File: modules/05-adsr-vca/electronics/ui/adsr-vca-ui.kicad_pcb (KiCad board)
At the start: 2 copper layers, 58 x 110 mm, 36 parts, among them J1 Conn_02x03_Odd_Even, J3 Conn_02x03_Odd_Even, J4 Conn_01x02, J5 Conn_01x06, J6 Conn_02x03_Odd_Even, J8 Conn_02x03_Odd_Even, Q1 2N3904, Q2 2N3906

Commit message: ADSR+VCA UI JLCPCB verified for 1.0
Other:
- board text added: "SHMØERGH MODULEUR"
- board text added: "SM-05 ADSR VCA V1.0 2025 DEC"
- board text removed: "HM-05 ADSR VCA V0.2 2025 OCT"
- board text removed: "SHMØERGH HOG MODULEUR"

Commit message: Fixed pot part number bug in ADSR+VCA
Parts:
- RV_ATTACK1, RV_DECAY1, RV_RELEASE1: value A500k -> A200k-1M
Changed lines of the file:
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@@
 			)
 		)
-		(property "Value" "A500k"
+		(property "Value" "A200k-1M"
 			(at 0.1 13.379024 180)
 			(layer "F.Fab")
@@
 			)
 		)
-		(property "Part URL" "https://mou.sr/4694GMU"
+		(property "Part URL" "https://mou.sr/3VpxrOs"
 			(at 0 0 0)
 			(unlocked yes)
@@
 			)
 		)
-		(property "Part no." "652-PTV09A4025FB104"
+		(property "Part no." "652-PTV09A4025FA105 "
 			(at 0 0 0)
 			(unlocked yes)
@@
 			)
 		)
-		(property "Part URL" ""
+		(property "Part URL" "https://mou.sr/3MWzgkZ"
 			(at 0 0 0)
 			(unlocked yes)
@@
 			)
 		)
-		(property "Vendor" ""
+		(property "Vendor" "Mouser"
 			(at 0 0 0)
 			(unlocked yes)
@@
 			)
 		)
+		(property "Part no." "603-MFR-25FRF52-47K"
+			(at 0 0 0)
+			(unlocked yes)
+			(layer "F.Fab")
+			(hide yes)
+			(effects
+				(font
+					(size 1 1)
+					(thickness 0.15)
+				)
+			)
+		)
 		(property ki_fp_filters "R_*")
 		(sheetname "/")
@@
 			)
 		)
-		(property "Part URL" ""
+		(property "Part URL" "https://mou.sr/4a8lju1"
 			(at 0 0 180)
 			(unlocked yes)
@@
 			)
 		)
-		(property "Vendor" ""
+		(property "Vendor" "Mouser"
 			(at 0 0 180)
 			(unlocked yes)
@@
 			)
 		)
+		(property "Part no." "637-2N3906"
+			(at 0 0 180)
+			(unlocked yes)
+			(layer "F.Fab")
+			(hide yes)
+			(effects
+				(font
+					(size 1 1)
+					(thickness 0.15)
+				)
+			)
+		)
 		(property ki_fp_filters "TO?92*")
 		(sheetname "/")
@@
 			)
 		)
-		(property "Part URL" ""
+		(property "Part URL" "https://mou.sr/4hEwI4G"
 			(at 0 0 90)
 			(unlocked yes)
@@
 			)
 		)
-		(property "Vendor" ""
+		(property "Vendor" "Mouser"
 			(at 0 0 90)
 			(unlocked yes)
@@
 			)
 		)
+		(property "Part no." "603-MFR-25FRF52100K"
+			(at 0 0 90)
+			(unlocked yes)
+			(layer "F.Fab")
+			(hide yes)
+			(effects
+				(font
+					(size 1 1)
+					(thickness 0.15)
+				)
+			)
+		)
 		(property ki_fp_filters "R_*")
 		(sheetname "/")
@@
 			)
 		)
-		(property "Part URL" ""
+		(property "Part URL" "https://mou.sr/4q072Ei"
 			(at 0 0 0)
 			(unlocked yes)
@@
 			)
 		)
-		(property "Vendor" ""
+		(property "Vendor" "Mouser"
 			(at 0 0 0)
 			(unlocked yes)
@@
 			)
 		)
+		(property "Part no." "603-MFR25SFTF52-4K7"
+			(at 0 0 0)
+			(unlocked yes)
+			(layer "F.Fab")
+			(hide yes)
+			(effects
+				(font
+					(size 1 1)
+					(thickness 0.15)
+				)
+			)
+		)
 		(property ki_fp_filters "R_*")
 		(sheetname "/")
@@
 			)
 		)
-		(property "Part URL" ""
+		(property "Part URL" "https://mou.sr/4febysZ"
 			(at 0 0 270)
 			(unlocked yes)
@@
 			)
 		)
-		(property "Vendor" ""
+		(property "Vendor" "Mouser"
 			(at 0 0 270)
 			(unlocked yes)
@@
 			)
 		)
+		(property "Part no." "637-2N3904"
+			(at 0 0 270)
+			(unlocked yes)
+			(layer "F.Fab")
+			(hide yes)
+			(effects
+				(font
+					(size 1 1)
+					(thickness 0.15)
+				)
+			)
+		)
 		(property ki_fp_filters "TO?92*")
 		(sheetname "/")
@@
 			)
 		)
-		(property "Value" "A500k"
+		(property "Value" "A200k-1M"
 			(at 0.1 13.379024 180)
 			(layer "F.Fab")
@@
 			)
 		)
-		(property "Part URL" "https://mou.sr/4694GMU"
+		(property "Part URL" "https://mou.sr/3VpxrOs"
 			(at 0 0 0)
 			(unlocked yes)
@@
 			)
 		)
-		(property "Part no." "652-PTV09A4025FB104"
+		(property "Part no." "652-PTV09A4025FA105 "
 			(at 0 0 0)
 			(unlocked yes)
@@
 			)
 		)
-		(property "Part URL" "https://mou.sr/4694GMU"
+		(property "Part URL" "https://mou.sr/45PU5oa"
 			(at 0 0 90)
 			(unlocked yes)
@@
 			)
 		)
-		(property "Part no." "652-PTV09A4025FB104"
+		(property "Part no." "652-PTA4432015CPB103 "
 			(at 0 0 90)
 			(unlocked yes)
@@
 			)
 		)
-		(property "Value" "A500k"
+		(property "Value" "A200k-1M"
 			(at 0.1 13.379024 180)
 			(layer "F.Fab")
@@
 			)
 		)
-		(property "Part URL" "https://mou.sr/4694GMU"
+		(property "Part URL" "https://mou.sr/3VpxrOs"
 			(at 0 0 0)
 			(unlocked yes)
@@
 			)
 		)
-		(property "Part no." "652-PTV09A4025FB104"
+		(property "Part no." "652-PTV09A4025FA105 "
 			(at 0 0 0)
 			(unlocked yes)
@@
 			)
 		)
-		(property "Part URL" ""
+		(property "Part URL" "https://mou.sr/4nM6IZz"
 			(at 0 0 0)
 			(unlocked yes)
@@
 			)
 		)
-		(property "Vendor" ""
+		(property "Vendor" "Mouser"
 			(at 0 0 0)
 			(unlocked yes)
@@
 			(at 0 0 0)
 			(unlocked yes)
+			(layer "F.Fab")
+			(hide yes)
+			(effects
+				(font
+					(size 1 1)
+					(thickness 0.15)
+				)
+			)
+		)
+		(property "Part no." "200-HTSW10208TSRA"
+			(at 0 0 0)
+			(unlocked yes)

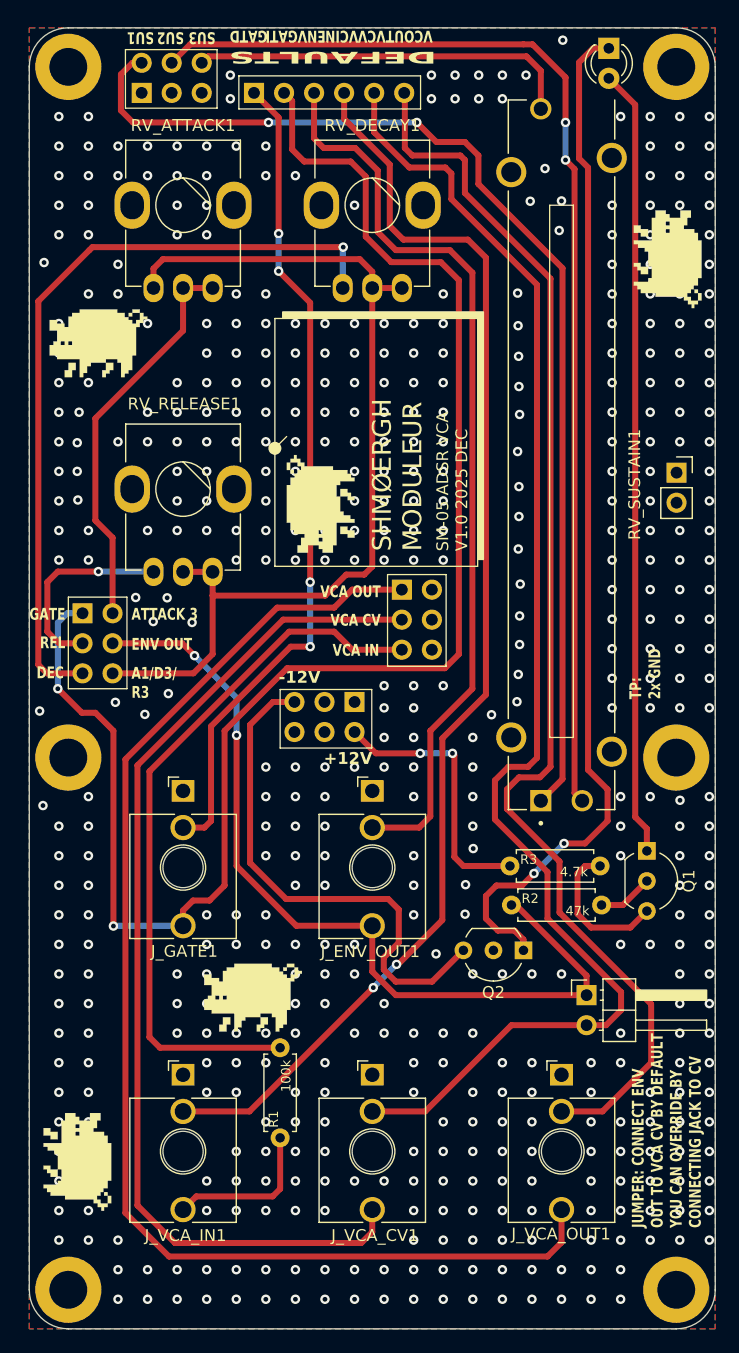
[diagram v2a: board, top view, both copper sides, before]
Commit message: Fixed missing resistor for VCA CV input
Boards before this commit missed a 200k resistor on the CV input of the VCA,
which caused the VCA to be very hot.

Additionally, we've added a small optional passive LP network to the CV input
to smoothen sudden changes on the CV input (which can cause very minor pops
on very short attack times for example).
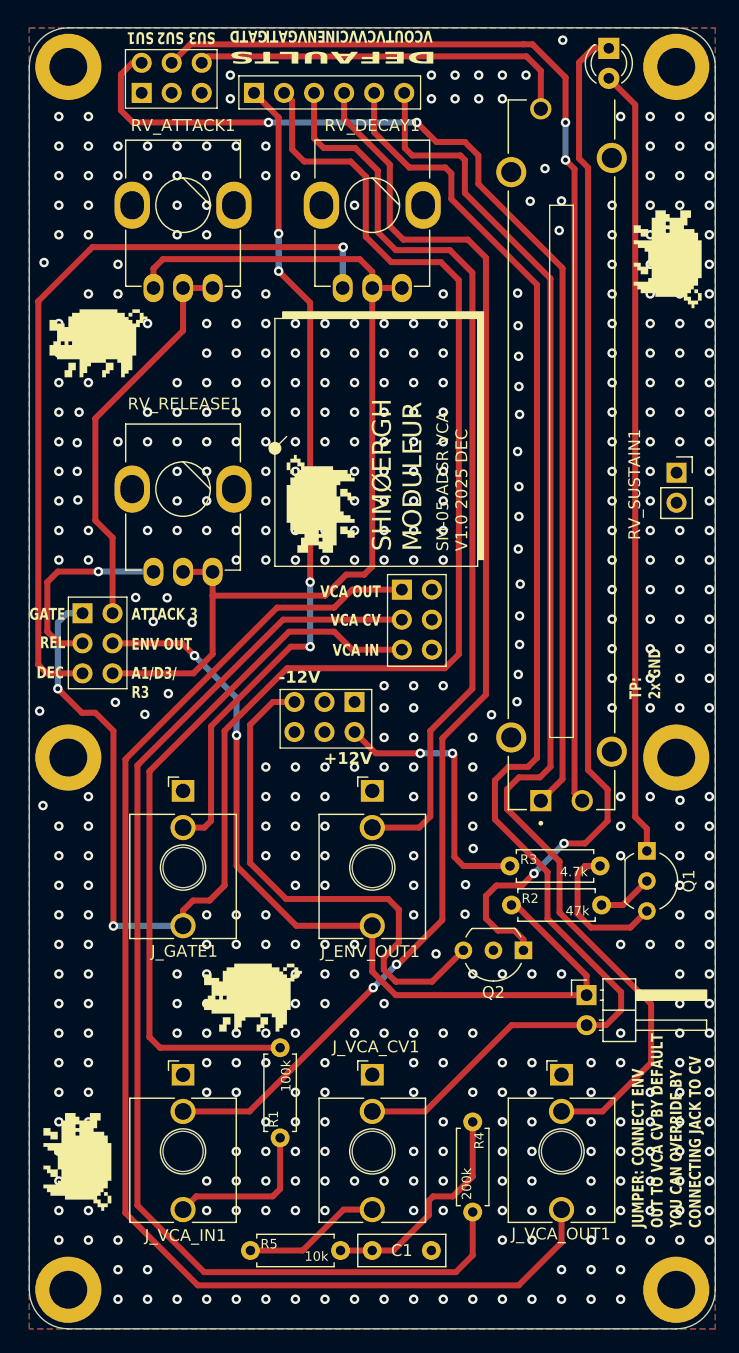
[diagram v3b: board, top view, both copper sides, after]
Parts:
- added C1: 100nF, Capacitor_THT:C_Rect_L7.2mm_W2.5mm_P5.00mm_FKS2_FKP2_MKS2_MKP2, F.Cu at (153.0, 147.4)
- added R4: 200k, Shmoergh_Custom_Footprints:R_Axial_DIN0207_L6.3mm_D2.5mm_P7.62mm_Horizontal, F.Cu at (161.5, 136.5)
- added R5: 10k, Shmoergh_Custom_Footprints:R_Axial_DIN0207_L6.3mm_D2.5mm_P7.62mm_Horizontal, F.Cu at (142.7, 147.4)
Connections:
- J_VCA_CV1 pad T: VCA_CV -> Net-(J_VCA_CV1-PadT)
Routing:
- net Net-(C1-Pad1): track 0.00 -> 19.1 mm
- net Net-(J_VCA_CV1-PadT): track 0.00 -> 11.7 mm
- net VCA_CV: track 88.1 -> 99.6 mm
- net VCA_OUT: track 109.3 -> 111.4 mm
- net GND: vias 521 -> 501

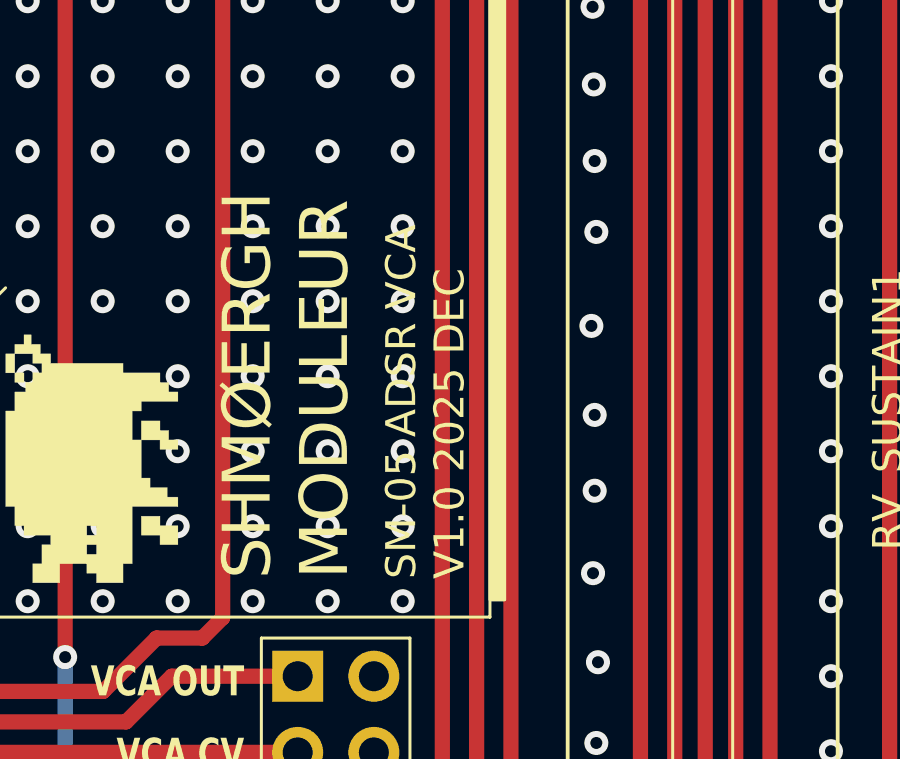
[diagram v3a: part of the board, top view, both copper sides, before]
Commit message: Updated VCA UI version to v1.1
This revision contains fix for missing resistor on VCA CV input,
and adds an optional LP filter for the CV input to avoid small pops
on sudden CV changes (e.g. very short attacks).
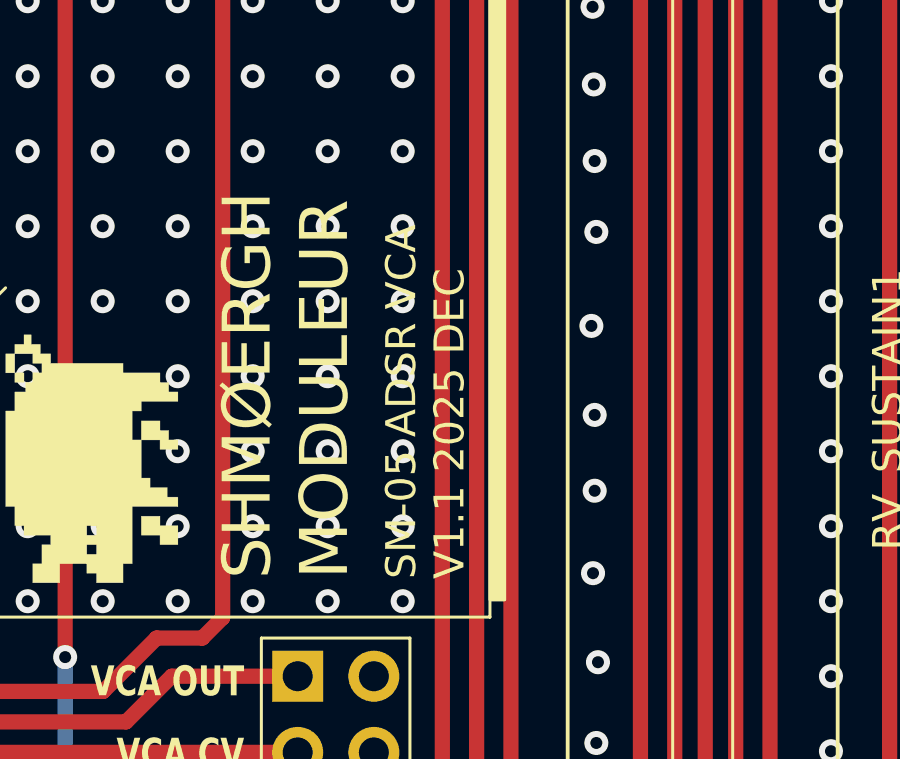
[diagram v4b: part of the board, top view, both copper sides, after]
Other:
- board text added: "SM-05 ADSR VCA V1.1 2025 DEC"
- board text removed: "SM-05 ADSR VCA V1.0 2025 DEC"
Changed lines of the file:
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@@
 		)
 	)
-	(gr_text "SM-05 ADSR VCA\nV1.0 2025 DEC"
+	(gr_text "SM-05 ADSR VCA\nV1.1 2025 DEC"
 		(at 161.1475 88.2595 90)
 		(layer "F.SilkS")
@@
 			(justify left bottom)
 		)
-		(render_cache "SM-05 ADSR VCA\nV1.0 2025 DEC" 90
+		(render_cache "SM-05 ADSR VCA\nV1.1 2025 DEC" 90
 			(polygon
 				(pts
@@
 			(polygon
 				(pts
-					(xy 160.086624 85.462186) (xy 160.850249 85.462186) (xy 160.850249 85.334936) (xy 160.595687 85.334936)
-					(xy 160.595687 85.207624) (xy 160.468436 85.207624) (xy 160.468436 85.334936) (xy 160.086624 85.334936)
-				)
-			)
-			(polygon
-				(pts
-					(xy 160.850249 85.334936) (xy 160.9775 85.334936) (xy 160.9775 84.953123) (xy 160.850249 84.953123)
-				)
-			)
-			(polygon
-				(pts
-					(xy 159.959312 85.334936) (xy 160.086624 85.334936) (xy 160.086624 84.953123) (xy 159.959312 84.953123)
-				)
-			)
-			(polygon
-				(pts
-					(xy 160.086624 84.953123) (xy 160.213874 84.953123) (xy 160.213874 85.080374) (xy 160.341186 85.080374)
-					(xy 160.341186 84.953123) (xy 160.850249 84.953123) (xy 160.850249 84.825811) (xy 160.086624 84.825811)
-				)
-			)
-			(polygon
-				(pts
-					(xy 160.341186 85.207624) (xy 160.468436 85.207624) (xy 160.468436 85.080374) (xy 160.341186 85.080374)
-				)
-			)
+					(xy 160.213874 85.207624) (xy 160.850249 85.207624) (xy 160.850249 85.462186) (xy 160.9775 85.462186)
+					(xy 160.9775 84.825811) (xy 160.850249 84.825811) (xy 160.850249 85.080374) (xy 159.959312 85.080374)
+					(xy 159.959312 85.207624) (xy 160.086624 85.207624) (xy 160.086624 85.462186) (xy 160.213874 85.462186)
+				)
+			)

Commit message: Added VCA output testpoint to UI board
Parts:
- added TP1: TestPoint, TestPoint:TestPoint_THTPad_2.0x2.0mm_Drill1.0mm, F.Cu at (164.3, 150.3)
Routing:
- net GND: vias 501 -> 500
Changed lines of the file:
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@@
 		(embedded_fonts no)
 	)
+	(footprint "TestPoint:TestPoint_THTPad_2.0x2.0mm_Drill1.0mm"
+		(layer "F.Cu")
+		(at 164.259 150.299)
+		(descr "THT rectangular pad as test Point, square 2.0mm_Drill1.0mm  side length, hole diameter 1.0mm")
+		(tags "test point THT pad rectangle square")
+		(property "Reference" "TP1"
+			(at 0 -1.998 0)
+			(layer "F.SilkS")
+			(effects
+				(font
+					(size 1 1)
+					(thickness 0.15)
+				)
+			)
+		)
+		(property "Value" "TestPoint"
+			(at 0 2.05 0)
+			(layer "F.Fab")
+			(effects
+				(font
+					(size 1 1)
+					(thickness 0.15)
+				)
+			)
+		)
+		(property "Datasheet" "~"
+			(at 0 0 0)
+			(unlocked yes)
+			(layer "F.Fab")
+			(hide yes)
+			(effects
+				(font
+					(size 1.27 1.27)
+					(thickness 0.15)
+				)
+			)
+		)
+		(property "Description" "test point"
+			(at 0 0 0)
+			(unlocked yes)
+			(layer "F.Fab")
+			(hide yes)
+			(effects
+				(font
+					(size 1.27 1.27)
+					(thickness 0.15)
+				)
+			)
+		)
+		(property "Part No." ""
+			(at 0 0 0)
+			(unlocked yes)
+			(layer "F.Fab")
+			(hide yes)
+			(effects
+				(font
+					(size 1 1)
+					(thickness 0.15)
+				)
+			)
+		)
+		(property "Part URL" ""
+			(at 0 0 0)
+			(unlocked yes)
+			(layer "F.Fab")
+			(hide yes)
+			(effects
+				(font
+					(size 1 1)
+					(thickness 0.15)
+				)
+			)
+		)
+		(property "Vendor" ""
+			(at 0 0 0)
+			(unlocked yes)
+			(layer "F.Fab")
+			(hide yes)
+			(effects
+				(font
+					(size 1 1)
+					(thickness 0.15)
+				)
+			)
+		)
+		(property "LCSC" ""
+			(at 0 0 0)
+			(unlocked yes)
+			(layer "F.Fab")
+			(hide yes)
+			(effects
+				(font
+					(size 1 1)
+					(thickness 0.15)
+				)
+			)
+		)
+		(property ki_fp_filters "Pin* Test*")
+		(sheetname "/")
+		(sheetfile "adsr-vca-ui.kicad_sch")
+		(attr exclude_from_pos_files)
+		(fp_line
+			(start -1.2 -1.2)
+			(end 1.2 -1.2)
+			(stroke
+				(width 0.12)
+				(type solid)
+			)
+			(layer "F.SilkS")
+		)
+		(fp_line
+			(start -1.2 1.2)
+			(end -1.2 -1.2)
+			(stroke
+				(width 0.12)
+				(type solid)
+			)
+			(layer "F.SilkS")
+		)
+		(fp_line
+			(start 1.2 -1.2)
+			(end 1.2 1.2)
+			(stroke
+				(width 0.12)
+				(type solid)
+			)
+			(layer "F.SilkS")
+		)
+		(fp_line
+			(start 1.2 1.2)
+			(end -1.2 1.2)
+			(stroke
+				(width 0.12)
+				(type solid)
+			)
+			(layer "F.SilkS")
+		)
+		(fp_line
+			(start -1.5 -1.5)
+			(end -1.5 1.5)
+			(stroke
+				(width 0.05)
+				(type solid)
+			)
+			(layer "F.CrtYd")
+		)
+		(fp_line
+			(start -1.5 -1.5)
+			(end 1.5 -1.5)
+			(stroke
+				(width 0.05)
+				(type solid)
+			)
+			(layer "F.CrtYd")
+		)
+		(fp_line
+			(start 1.5 1.5)
+			(end -1.5 1.5)
+			(stroke
+				(width 0.05)
+				(type solid)
+			)
+			(layer "F.CrtYd")
+		)
+		(fp_line
+			(start 1.5 1.5)
+			(end 1.5 -1.5)
+			(stroke
+				(width 0.05)
+				(type solid)
+			)
+			(layer "F.CrtYd")
+		)
+		(fp_text user "${REFERENCE}"
+			(at 0 -2 0)
+			(layer "F.Fab")
+			(effects
+				(font
+					(size 1 1)
+					(thickness 0.15)
+				)
+			)
+		)
+		(pad "1" thru_hole rect
+			(at 0 0)
+			(size 2 2)
+			(drill 1)
+			(layers "*.Cu" "*.Mask")
+			(remove_unused_layers no)
+			(net 6 "VCA_OUT")
+			(pinfunction "1")
+			(pintype "passive")
+		)
+		(embedded_fonts no)
+	)
 	(footprint "Shmoergh_Custom_Footprints:Potentiometer_Bourns_Single-PTV09A"
 		(layer "F.Cu")
@@
 		(size 0.8)
 		(drill 0.4)
-		(layers "F.Cu" "B.Cu")
-		(free yes)
-		(net 3)
-	)
-	(via
-		(at 164 151.5)
-		(size 0.8)
-		(drill 0.4)
